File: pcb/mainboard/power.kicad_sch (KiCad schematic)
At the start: 16 parts

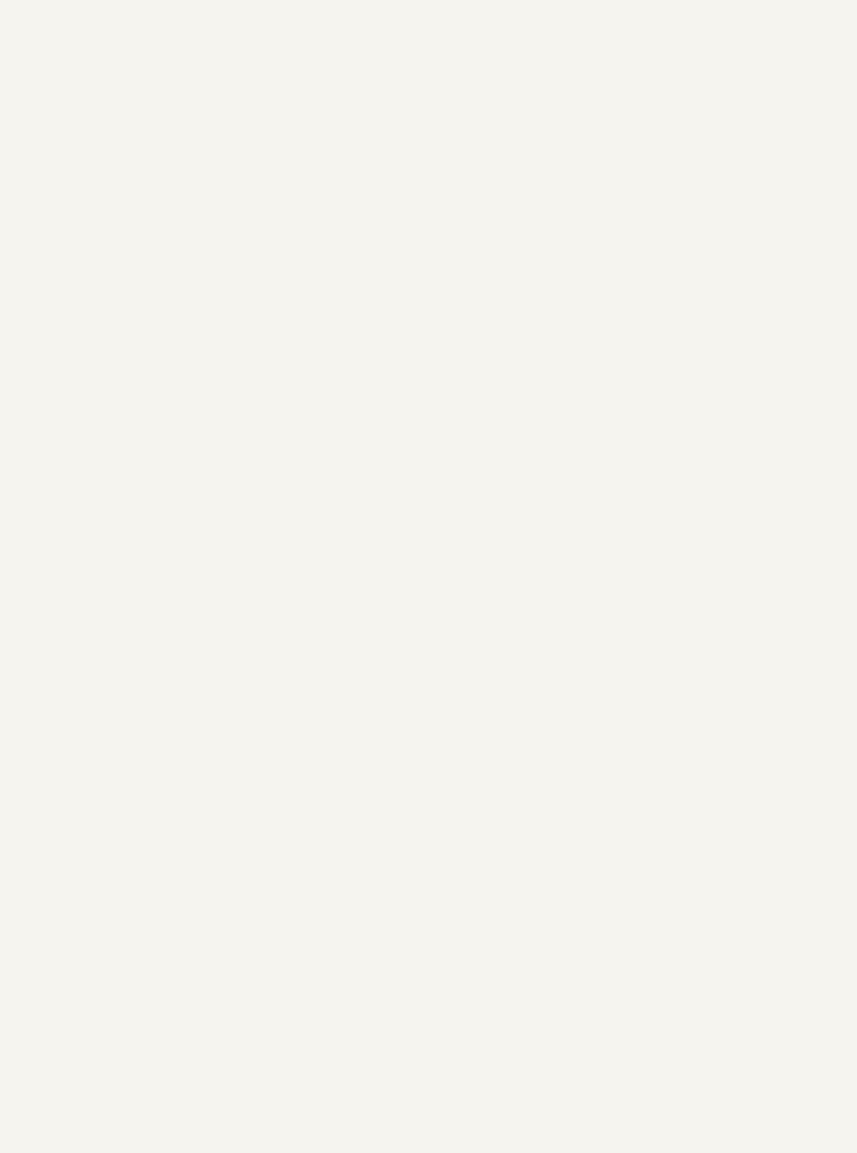
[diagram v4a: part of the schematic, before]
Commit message: - pcb: working on power supply
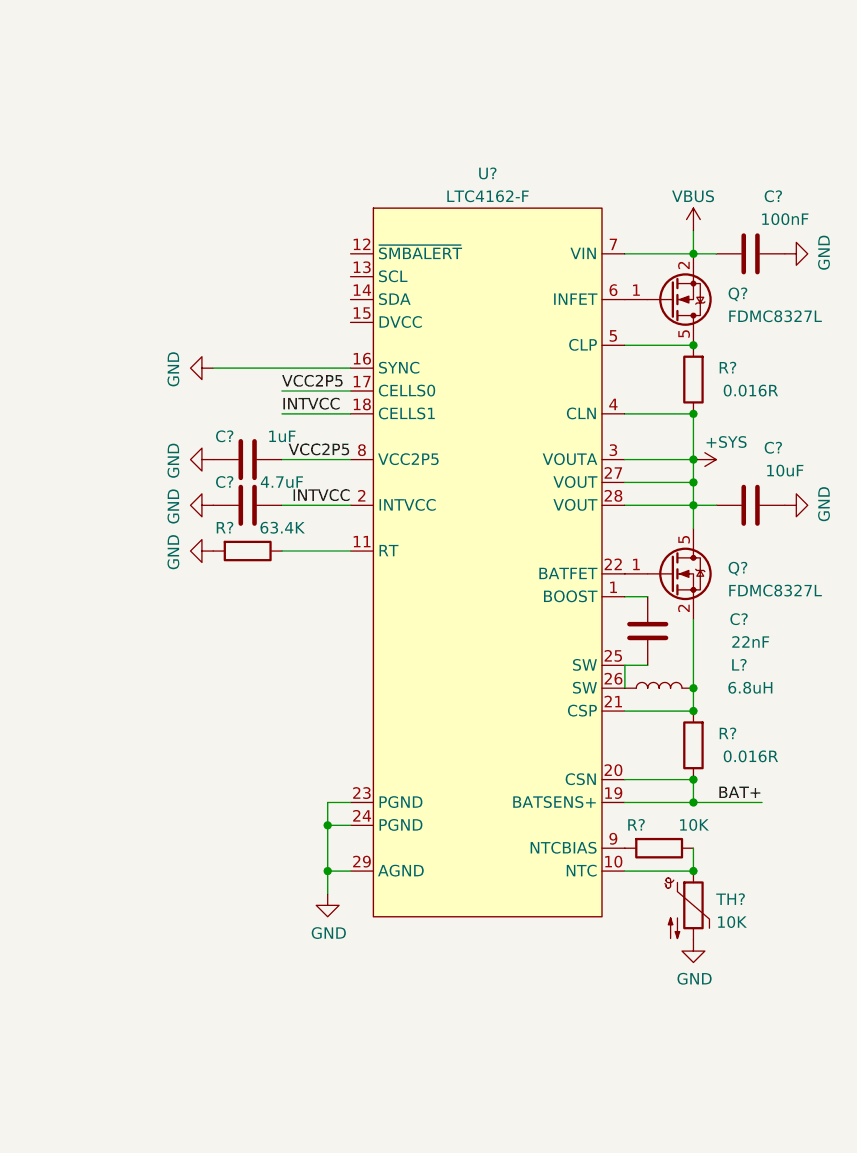
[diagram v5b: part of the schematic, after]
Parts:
- added C?: 1uF, Capacitor_SMD:C_0402_1005Metric, symbol Device:C
- added C?: 100nF, Capacitor_SMD:C_0402_1005Metric, symbol Device:C
- added C?: 22nF, Capacitor_SMD:C_0402_1005Metric, symbol Device:C
- added C?: 10uF, Capacitor_SMD:C_0402_1005Metric, symbol Device:C
- added C?: 4.7uF, Capacitor_SMD:C_0402_1005Metric, symbol Device:C
- added L?: 6.8uH, symbol Device:L
- added Q? (x2): FDMC8327L, Package_SON:Diodes_PowerDI3333-8, symbol symbols:FDMC8327L
- added R?: 63.4K, Resistor_SMD:R_0402_1005Metric, symbol Device:R
- added R? (x2): 0.016R, Resistor_SMD:R_0402_1005Metric, symbol Device:R
- added R?: 10K, Resistor_SMD:R_0402_1005Metric, symbol Device:R
- added TH?: 10K, symbol Device:Thermistor_NTC
- added U?: LTC4162-F, Package_DFN_QFN:QFN-28-1EP_4x5mm_P0.5mm_EP2.65x3.65mm_ThermalVias, symbol symbols:LTC4162-F
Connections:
- net GND: now also C?.1, C?.1, C?.1, C?.1, R?.2, TH?.2, U?.16 (SYNC), U?.23 (PGND), U?.24 (PGND), U?.29 (AGND)
- new net: R?.1, U?.11 (RT)
- new net: L?.2, Q?.2 (S), Q?.3 (S), Q?.4 (S), R?.2, U?.21 (CSP)
- new net: C?.2, L?.1, U?.25 (SW), U?.26 (SW)
- new net: Q?.1 (G), U?.6 (INFET)
- new net: Q?.5 (D), Q?.6 (D), Q?.7 (D), Q?.8 (D), R?.2, U?.5 (CLP)
- new net: Q?.1 (G), U?.22 (BATFET)
- new net: R?.1, TH?.1, U?.10 (NTC)
- new net: R?.2, U?.9 (NTCBIAS)
- new net: C?.1, U?.1 (BOOST)
- new net +SYS: C?.2, Q?.5 (D), Q?.6 (D), Q?.7 (D), Q?.8 (D), R?.1, U?.27 (VOUT), U?.28 (VOUT), U?.3 (VOUTA), U?.4 (CLN)
- new net BAT+: R?.1, U?.19 (BATSENS+), U?.20 (CSN)
- new net INTVCC: C?.2, U?.18 (CELLS1), U?.2 (INTVCC)
- new net VBUS: C?.2, Q?.2 (S), Q?.3 (S), Q?.4 (S), U?.7 (VIN)
- new net VCC2P5: C?.2, U?.17 (CELLS0), U?.8 (VCC2P5)

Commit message: - pcb: r0p1 sch draft
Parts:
- removed C? (x2): 470nF, Capacitor_SMD:C_0402_1005Metric, symbol Device:C
- removed L?: 2.2uH, Inductor_SMD:L_Vishay_IHLP-1212, symbol Device:L
- removed R?: 10K, Resistor_SMD:R_0402_1005Metric, symbol Device:R
- removed R?: 20K, Resistor_SMD:R_0402_1005Metric, symbol Device:R
- removed U?: SY8008, Package_TO_SOT_SMD:TSOT-23-5, symbol symbols:SY8008
- added BT_Backup1: CR2032, footprints:BatteryHolder_CR1220, symbol Device:Battery_Cell
- added C1, C2, C3, C4, C5, C6: 4.7uF, Capacitor_SMD:C_0805_2012Metric, symbol Device:C
- added C10, C11, C12, C13, C14, C15, C16, C17, C18, C7, C8, C9: 100nF, Capacitor_SMD:C_0603_1608Metric, symbol Device:C
- added C19, C20, C21, C22, C23, C24: 10uF, Capacitor_SMD:C_0603_1608Metric, symbol Device:C
- added C25, C26, C27, C28, C29, C30, C42: 10uF, Capacitor_SMD:C_Elec_5x5.8, symbol Device:C
- added C34: 10nF, Capacitor_SMD:C_Elec_5x5.8, symbol Device:C
- added C37, C38: 100nF, Capacitor_SMD:C_0402_1005Metric, symbol Device:C
- added C39: 10pF, Capacitor_SMD:C_0402_1005Metric, symbol Device:C
- added C45, C46, C47, C48, C49, C50, C51, C52, C53, C54, C55, C56, C57, C59, C62, C63, C64, C65, C66, C67: 220nF, Capacitor_SMD:C_0402_1005Metric, symbol Device:C
- added C58, C68, C69, C70: 2.2uF, Capacitor_SMD:C_0402_1005Metric, symbol Device:C
- added C60, C61: 22uF, Capacitor_SMD:C_0603_1608Metric, symbol Device:C
- added D1, D2: 1N5819, Diode_SMD:D_SOD-123, symbol Device:D_Schottky
- added L1, L2, L3, L4, L5, L6: 4.7uH, Inductor_SMD:L_Vishay_IHLP-1212, symbol Device:L
- added L8: 10uH, symbol Device:L
- added L9: 120R, Inductor_SMD:L_0402_1005Metric, symbol Device:L
- added R1, R16: 200K/1%, Resistor_SMD:R_0603_1608Metric, symbol Device:R
- added R10, R12, R2, R6, R8: 27K/1%, Resistor_SMD:R_0603_1608Metric, symbol Device:R
- added R11: 34.8K/1%, Resistor_SMD:R_0603_1608Metric, symbol Device:R
- added R13: 100K, Resistor_SMD:R_0402_1005Metric, symbol Device:R
- added R15: 18.2K, Resistor_SMD:R_0603_1608Metric, symbol Device:R
- added R19: 649K/1%, Resistor_SMD:R_0402_1005Metric, symbol Device:R
- added R3: 20K/1%, Resistor_SMD:R_0603_1608Metric, symbol Device:R
- added R4: 10K/1%, Resistor_SMD:R_0603_1608Metric, symbol Device:R
- added R5: 121K/1%, Resistor_SMD:R_0603_1608Metric, symbol Device:R
- added R7, R9: 22.6K/1%, Resistor_SMD:R_0603_1608Metric, symbol Device:R
- added U1, U2, U3, U4, U5, U6: SY8120, Package_TO_SOT_SMD:TSOT-23-6, symbol symbols:SY8120
- added U10: MCIMX7S5EVM08SC, footprints:BGA-541_25x25_19.0x19.0mm, symbol symbols:MCIMX7S5EVM08SC
- added U7: LT8606, Package_SO:MSOP-10-1EP_3x3mm_P0.5mm_EP1.68x1.88mm_ThermalVias, symbol symbols:LT8606
- gave numbers to parts that had none: 24
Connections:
- net +1V8: now also C20.2, C26.2, C59.1, L2.2, L9.1, R3.2, U10.V8 (FUSE_FSOURCE), U10.W6 (VDD_LPSR_IN)
- net +3V3: now also C21.2, C27.2, C63.1, C64.1, D1.2 (A), L3.2, R5.2, U10.P8 (NVCC_GPIO1), U10.T8 (NVCC_GPIO2)
- net +5V: now also C19.2, C25.2, L1.2, R1.2
- net +SYS: now also C1.2, C10.2, C11.2, C12.2, C2.2, C3.2, C4.2, C5.2, C6.2, C7.2, C8.2, C9.2, U1.5 (VIN), U2.5 (VIN), U3.5 (VIN), U4.5 (VIN), U5.5 (VIN), U6.5 (VIN), U7.10 (EN/UV), U7.9 (VIN)
- net GND: now also BT_Backup1.2 (-), C1.1, C10.1, C11.1, C12.1, C19.1, C2.1, C20.1, C21.1, C22.1, C23.1, C24.1, C25.1, C26.1, C27.1, C28.1, C29.1, C3.1, C30.1, C34.1, C37.1, C4.1, C42.1, C45.2, C46.2, C47.2, C48.2, C49.2, C5.1, C50.2, C51.2, C52.2, C53.2, C54.2, C55.2, C56.2, C57.2, C58.2, C59.2, C6.1, C60.2, C61.2, C62.2, C63.2, C64.2, C65.1, C66.1, C67.1, C68.1, C69.1, C7.1, C70.1, C8.1, C9.1, R10.1, R12.1, R15.1, R16.1, R2.1, R4.1, R6.1, R8.1, U1.2 (GND), U10.A1 (GND), U10.A13 (GND), U10.A17 (GND), U10.A21 (GND), U10.A25 (GND), U10.A3 (GND), U10.A6 (GND), U10.A9 (GND), U10.AA1 (GND), U10.AA10 (PCIE_VP), U10.AA11 (PCIE_VP_TX), U10.AA12 (PCIE_VP_RX), U10.AA15 (GND), U10.AA2 (GND), U10.AA23 (GND), U10.AA6 (GND), U10.AA8 (GND), U10.AB12 (GND), U10.AB4 (GND), U10.AB5 (GND), U10.AB7 (GND), U10.AB9 (GND), U10.AC12 (GND), U10.AC15 (GND), U10.AC17 (GND), U10.AC19 (GND), U10.AC21 (GND), U10.AC23 (GND), U10.AC6 (GND), U10.AC9 (GND), U10.AD12 (GND), U10.AD2 (GND), U10.AD5 (GND), U10.AD7 (GND), U10.AD9 (GND), U10.AE1 (GND), U10.AE12 (GND), U10.AE24 (GND), U10.AE25 (GND), U10.AE5 (GND), U10.AE7 (GND), U10.AE9 (GND), U10.B13 (GND), U10.B17 (GND), U10.B21 (GND), U10.B3 (GND), U10.B6 (GND), U10.B9 (GND), U10.C13 (GND), U10.C15 (GND), U10.C16 (GND), U10.C18 (GND), U10.C19 (GND), U10.C9 (GND), U10.D1 (GND), U10.D10 (GND), U10.D2 (GND), U10.D22 (GND), U10.D4 (GND), U10.D7 (GND), U10.F11 (GND), U10.F13 (GND), U10.F7 (GND), U10.F8 (GND), U10.G11 (GND), U10.G13 (GND), U10.G15 (GND), U10.G17 (GND), U10.G19 (GND), U10.G22 (GND), U10.G4 (GND), U10.G7 (GND), U10.G9 (GND), U10.H1 (GND), U10.H12 (USB_VDD_H_1P2), U10.H2 (GND), U10.J19 (GND), U10.J7 (GND), U10.K10 (GND), U10.K12 (GND), U10.K14 (GND), U10.K16 (GND), U10.K22 (GND), U10.K4 (GND), U10.L11 (GND), U10.L13 (GND), U10.L15 (GND), U10.L19 (GND), U10.L7 (GND), U10.M10 (GND), U10.M12 (GND), U10.M14 (GND), U10.M16 (GND), U10.M24 (GND), U10.M25 (GND), U10.N11 (GND), U10.N13 (GND), U10.N15 (GND), U10.N19 (GND), U10.N4 (GND), U10.N7 (GND), U10.P10 (GND), U10.P12 (GND), U10.P14 (GND), U10.P16 (GND), U10.R11 (GND), U10.R13 (GND), U10.R15 (GND), U10.R19 (GND), U10.R20 (GND), U10.R21 (GND), U10.R23 (GND), U10.R7 (GND), U10.T10 (GND), U10.T12 (GND), U10.T14 (GND), U10.T16 (GND), U10.T20 (GND), U10.T4 (GND), U10.U11 (GND), U10.U19 (GND), U10.U20 (GND), U10.U23 (GND), U10.U7 (GND), U10.V20 (GND), U10.W1 (GND), U10.W11 (GND), U10.W13 (GND), U10.W15 (GND), U10.W17 (GND), U10.W19 (GND), U10.W2 (GND), U10.W20 (GND), U10.W23 (GND), U10.W4 (GND), U10.W7 (GND), U10.W9 (GND), U10.Y10 (PCIE_VPH), U10.Y11 (PCIE_VPH_TX), U10.Y12 (PCIE_VPH_RX), U10.Y13 (GND), U10.Y14 (GND), U10.Y15 (GND), U10.Y16 (GND), U10.Y17 (GND), U10.Y18 (GND), U10.Y19 (GND), U10.Y6 (GND), U2.2 (GND), U3.2 (GND), U4.2 (GND), U5.2 (GND), U6.2 (GND), U7.11 (GND)
- net EC_INT: now reaches U8.12 (~SMBALERT)
- net EC_I2C_SDA: now reaches U8.13 (SCL)
- net EC_I2C_SCL: now reaches U8.14 (SDA)
- net +3V3_SB: now reaches U8.15 (DVCC)
- net +3V3_SB: now also C39.1, C42.2, L8.2, R13.2, R19.1
- new net: C17.1, L5.1, U5.6 (SW)
- new net: R5.1, R6.2, U3.3 (FB)
- new net: C18.2, U6.1 (BS)
- new net: R11.1, R12.2, U6.3 (FB)
- new net: C18.1, L6.1, U6.6 (SW)
- new net: C14.1, L2.1, U2.6 (SW)
- new net: C15.1, L3.1, U3.6 (SW)
- new net: C39.2, R16.2, R19.2, U7.6 (FB)
- new net: R1.1, R2.2, U1.3 (FB)
- new net: BT_Backup1.1 (+), D2.2 (A)
- new net: R7.1, R8.2, U4.3 (FB)
- new net: C69.2, U10.AC5 (VDD_LPSR_1P0_CAP)
- new net: C15.2, U3.1 (BS)
- new net: C17.2, U5.1 (BS)
- new net: R10.2, R9.1, U5.3 (FB)
- new net: C13.1, L1.1, U1.6 (SW)
- new net: C16.2, U4.1 (BS)
- new net: C16.1, L4.1, U4.6 (SW)
- new net: R15.2, U7.4 (RT)
- new net: C34.2, U7.7 (TR/SS)
- new net: C66.2, U10.V3 (VDDA_1P0_CAP)
- new net: C14.2, U2.1 (BS)
- new net: C65.2, U10.AA9 (VDDD_1P0_CAP)
- new net: C68.2, U10.AE8 (VDD_SNVS_1P8_CAP)
- new net: C67.2, U10.H18 (MIPI_VREG_0P4V)
- new net: C70.2, U10.V10 (PVCC_GPIO_CAP)
- new net: C38.1, L8.1, U7.2 (SW)
- new net: C38.2, U7.1 (BST)
- new net: R3.1, R4.2, U2.3 (FB)
- new net: C13.2, U1.1 (BS)
- new net: C37.2, U7.3 (INTVcc)
- new net +1V0: C22.2, C28.2, C45.1, C46.1, C47.1, C48.1, C49.1, C50.1, C51.1, C52.1, C53.1, C55.1, C56.1, C57.1, C60.1, C61.1, C62.1, L4.2, R7.2, U10.C14 (VDD_SOC_IN), U10.D14 (VDD_SOC_IN), U10.F18 (VDD_SOC_IN), U10.F19 (VDD_SOC_IN), U10.F3 (VDD_SOC_IN), U10.F4 (VDD_SOC_IN), U10.J3 (VDD_SOC_IN), U10.J4 (VDD_SOC_IN), U10.M3 (VDD_SOC_IN), U10.M4 (VDD_SOC_IN), U10.P18 (VDD_SOC_IN), U10.R17 (VDD_SOC_IN), U10.R3 (VDD_SOC_IN), U10.R4 (VDD_SOC_IN), U10.T18 (VDD_SOC_IN), U10.U13 (VDD_SOC_IN), U10.U15 (VDD_SOC_IN), U10.U17 (VDD_SOC_IN), U10.V12 (VDD_SOC_IN), U10.V14 (VDD_SOC_IN), U10.V16 (VDD_SOC_IN), U10.V18 (VDD_SOC_IN)
- new net +1V35: C24.2, C30.2, L6.2, R11.2
- new net +1V8A: C54.1, C58.1, L9.2, U10.V6 (VDDA_1P8), U10.W5 (VDDA_1P8)
- new net +RTC: D1.1 (K), D2.1 (K), U10.AD8 (VDD_SNVS_IN)
- new net 1V0_ARM: C23.2, C29.2, L5.2, R9.2, U10.C17 (VDD_ARM_IN), U10.C20 (VDD_ARM_IN), U10.D17 (VDD_ARM_IN), U10.D20 (VDD_ARM_IN), U10.F22 (VDD_ARM_IN), U10.F23 (VDD_ARM_IN), U10.J22 (VDD_ARM_IN), U10.J23 (VDD_ARM_IN)
- new net 5V_EN: U1.4 (RUN)
- new net ARM_EN: U5.4 (RUN)
- new net PWR_EN: U2.4 (RUN), U3.4 (RUN), U4.4 (RUN), U6.4 (RUN)
- new net SB_PG: R13.1, U7.8 (PG)
- no-connect marks 0 -> 6
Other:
- note added: "CAP for VDD_ARM"
- note added: "CAP for VDD_SOC"
- moved on the sheet: C31, C32, C33, C35, C36, C40, C41, C43, C44, L7, Q1, Q2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

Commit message: - pcb: start r0p1 layout
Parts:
- removed BT_Backup1: CR2032, footprints:BatteryHolder_CR1220, symbol Device:Battery_Cell
- removed D1, D2: 1N5819, Diode_SMD:D_SOD-123, symbol Device:D_Schottky
- added C71, C72, C73, C74, C75: 220nF, Capacitor_SMD:C_0402_1005Metric, symbol Device:C
- C1, C2, C3, C4, C5, C6: value 4.7uF -> 4.7uF/25V
- C25, C26, C27, C28, C29, C30, C42: footprint Capacitor_SMD:C_Elec_5x5.8 -> Capacitor_SMD:C_0603_1608Metric
- C33: footprint Capacitor_SMD:C_0402_1005Metric -> Capacitor_SMD:C_0603_1608Metric
- C34: footprint Capacitor_SMD:C_Elec_5x5.8 -> Capacitor_SMD:C_0402_1005Metric
- C41: value 10uF -> 10uF/25V; footprint Capacitor_SMD:C_0402_1005Metric -> Capacitor_SMD:C_0805_2012Metric
- L7, L8: footprint (none) -> Inductor_SMD:L_Vishay_IHLP-1212
- L9: footprint Inductor_SMD:L_0402_1005Metric -> Inductor_SMD:L_0603_1608Metric
- R1, R10, R11, R12, R16, R17, R18, R2, R23, R24, R3, R4, R5, R6, R7, R8, R9: footprint Resistor_SMD:R_0603_1608Metric -> Resistor_SMD:R_0402_1005Metric
- R15: value 18.2K -> 20K/1%; footprint Resistor_SMD:R_0603_1608Metric -> Resistor_SMD:R_0402_1005Metric
- TH1: footprint (none) -> Resistor_SMD:R_0402_1005Metric
- renumbered U10 to U101
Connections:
- net +RTC is gone; now on net +3V3_SB: U101.AD8 (VDD_SNVS_IN)
- net +1V0: now also C71.1, C72.1, C73.1, C74.1, C75.1; no longer C45.1, C48.1, C51.1, C55.1, C60.1
- net +SYS: no longer Q2.6 (D), Q2.7 (D), Q2.8 (D)
- net 1V0_ARM: now also C45.1, C48.1, C51.1, C55.1, C60.1
- net GND: now also C71.2, C72.2, C73.2, C74.2, C75.2
- net VBUS: now also Q1.1 (S); no longer Q1.4 (S)
- net at L7.2, Q2.2 (S), Q2.3 (S)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: now also Q2.1 (S); no longer Q2.4 (S)
- net at U8.6 (INFET): now also Q1.4 (G); no longer Q1.1 (G)
- net at Q1.5 (D), R21.2, U8.5 (CLP): no longer Q1.6 (D), Q1.7 (D), Q1.8 (D)
- net at U8.22 (BATFET): now also Q2.4 (G); no longer Q2.1 (G)
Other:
- company: Copyright EI-2030 2021. -> Copyright EI-2030 2021. / Engineer: Wenting Zhang
- title: Archer -> Archer Mainboard
- moved on the sheet: C45, C46, C47, C48, C49, C50, C51, C52, C53, C55, C56, C57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

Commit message: - pcb: components placed
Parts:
- removed TH1: 10K, Resistor_SMD:R_0402_1005Metric, symbol Device:Thermistor_NTC
- added C76, C78, C79: 220nF, Capacitor_SMD:C_0402_1005Metric, symbol Device:C
- added C77, C80: 2.2uF, Capacitor_SMD:C_0402_1005Metric, symbol Device:C
- added C81: 1uF, Capacitor_SMD:C_0402_1005Metric, symbol Device:C
- added J1: Conn_01x10_MountingPin, Connector_FFC-FPC:Hirose_FH12-10S-0.5SH_1x10-1MP_P0.50mm_Horizontal, symbol Connector_Generic_MountingPin:Conn_01x10_MountingPin
- C10, C11, C12, C13, C14, C15, C16, C17, C18, C7, C8, C9: footprint Capacitor_SMD:C_0603_1608Metric -> Capacitor_SMD:C_0402_1005Metric
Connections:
- net +3V3: no longer C31.1, C35.1, U9.1 (VIN), U9.3 (EN)
- net +5V: now also C31.1, C35.1, U9.1 (VIN), U9.3 (EN)
- net +SYS: now also C81.2
- net BAT+: now also J1.1 (Pin_1), J1.2 (Pin_2), J1.3 (Pin_3), J1.4 (Pin_4)
- net GND: now also C76.1, C77.1, C78.1, C79.1, C80.1, C81.1, J1.10 (Pin_10), J1.6 (Pin_6), J1.7 (Pin_7), J1.8 (Pin_8), J1.9 (Pin_9), J1.MP (MountPin); no longer U101.AA10 (PCIE_VP), U101.AA11 (PCIE_VP_TX), U101.AA12 (PCIE_VP_RX), U101.Y10 (PCIE_VPH), U101.Y11 (PCIE_VPH_TX), U101.Y12 (PCIE_VPH_RX)
- net BAT_NTC: now reaches R20.1, U8.10 (NTC)
- net BAT_NTC: now also J1.5 (Pin_5)
- net at C65.2, U101.AA9 (VDDD_1P0_CAP): now also U101.AA10 (PCIE_VP), U101.AA11 (PCIE_VP_TX), U101.AA12 (PCIE_VP_RX), U101.J15 (VDD_MIPI_1P0), U101.J17 (VDD_MIPI_1P0), C76.2, C77.2
- net at U101.J13 (VDDA_MIPI_1P8): now also U101.Y10 (PCIE_VPH), U101.Y11 (PCIE_VPH_TX), U101.Y12 (PCIE_VPH_RX), U101.Y9 (VDDA_PHY_1P8), C78.2, C79.2, C80.2
- net +VCCIO_WL renamed +VCCIO_SD
- no-connect marks 6 -> 2
